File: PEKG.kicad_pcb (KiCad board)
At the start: 2 copper layers, 90 x 45 mm, 108 parts, among them J1 AudioJack4, J2 AudioJack3, U1 TL072, U12 NCS21802DMR2G, U13 NCS21802DMR2G, U2 TL072, U3 INA350CDSIDDFR, U7 TLV61070ADBVR, U8 NCS21802DMR2G

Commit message: dfs
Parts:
- BT1: footprint Battery:BatteryHolder_Keystone_2462_2xAA -> PEKG:battery_holder
- moved BT1 3.01 mm to (120.2, 129.6)
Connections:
- C47 pad 2: Net-(U7-EN) -> VBAT
- L2 pad 1: Net-(U7-EN) -> VBAT
- L3 pad 1: Net-(U7-EN) -> VBAT
- U7 pad 3: Net-(U7-EN) -> VBAT
- U7 pad 6: Net-(U7-EN) -> VBAT
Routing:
- net GND: vias 0 -> 171
- net (no net): vias 171 -> 0

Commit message: Schematic done.
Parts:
- removed C48: 10u, Resistor_SMD:R_1206_3216Metric_Pad1.30x1.75mm_HandSolder
- removed L2: 4.7u, Inductor_THT:L_Radial_D7.5mm_P3.50mm_Fastron_07P
- removed TP10: TestPoint, TestPoint:TestPoint_Pad_D3.0mm
- added JP10: Jumper_2_Open, Jumper:SolderJumper-2_P1.3mm_Open_RoundedPad1.0x1.5mm, F.Cu at (141.8, 119.1)
- added JP9: Jumper_2_Bridged, Jumper:SolderJumper-2_P1.3mm_Bridged_RoundedPad1.0x1.5mm, F.Cu at (135.3, 128.7)
- added R12: 10k, Resistor_SMD:R_0603_1608Metric_Pad0.98x0.95mm_HandSolder, F.Cu at (186.2, 128.6)
- added R2: 100, Resistor_SMD:R_0603_1608Metric_Pad0.98x0.95mm_HandSolder, F.Cu at (182.9, 128.6)
- C46, G***, U3: moved to F.Cu
- J1: footprint Connector_Audio:Jack_3.5mm_CUI_SJ1-3524N_Horizontal -> PEKG:Jack_3.5mm_4pole
- J2: value AudioJack3 -> AudioJack3_SwitchTR; footprint PEKG:Jack_3.5mm_CUI_SJ1-3523N_Horizontal -> PEKG:Jack_3.5mm_CUI_SJ1-3525N_Horizontal
- U1, U2: value TL072 -> TLV9062
- U7: footprint Package_TO_SOT_SMD:SOT-23-6 -> Package_TO_SOT_SMD:SOT-23-6_Handsoldering
- moved TP6 87.3 mm to (122.5, 133.2)
- moved TP8 86.9 mm to (122.5, 141.2)
- moved TP9 85.8 mm to (122.5, 137.2)
- moved R60 83.3 mm to (134.5, 122.1), turned to 90 degrees
- moved TP7 81.3 mm to (126.7, 120.3)
- moved TP5 80.9 mm to (125.3, 113.0)
- moved R61 68.1 mm to (149.7, 123.2), turned to 90 degrees
- moved TP4 67.7 mm to (135.3, 133.2)
- moved TP3 64.9 mm to (139.0, 114.4)
- moved TP11 61.5 mm to (152.7, 127.2)
- moved R59 55.2 mm to (162.9, 112.9), turned to -90 degrees
- moved R58 53.5 mm to (164.4, 112.9), turned to -90 degrees
- moved U7 41.3 mm to (169.0, 132.2), turned to 180 degrees
- moved R63 40.5 mm to (171.6, 129.6), turned to 180 degrees
- moved R62 37.0 mm to (168.3, 129.6), turned to 180 degrees
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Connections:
- net 2.5V renamed V_{ref}
- net Net-(JP8-A) renamed /SW_OUT
- net Net-(U7-FB) renamed /FB
- net Net-(U7-SW) renamed /SW
- net VBUS renamed V_{cc}
- C15 pad 1: GAIN_500_OUTPUT -> Net-(JP9-A)
- C21 pad 1: GAIN_500_OUTPUT -> Net-(JP10-A)
- C22 pad 1: Earth -> GND
- C41 pad 1: Earth -> GND
- C47 pad 1: Earth -> GND
- R29 pad 2: GAIN_500_OUTPUT -> Net-(JP9-A)
- R57 pad 2: GAIN_500_OUTPUT -> Net-(JP10-A)
- R61 pad 2: GAIN_500_OUTPUT -> Net-(JP10-A)
- R63 pad 1: Earth -> GND
- TP4 pad 1: GAIN_500_OUTPUT -> Net-(JP9-A)
- U1 pad 7: GAIN_500_OUTPUT -> Net-(JP10-A)
- U12 pad 1: GAIN_500_OUTPUT -> Net-(JP9-A)
- U7 pad 2: Earth -> GND
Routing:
- net /TOP: track 0.00 -> 53.7 mm, vias 0 -> 3
- net /BOTTOM: track 0.00 -> 39.2 mm, vias 0 -> 2
- net COMMON_INPUT_LEVEL: track 0.00 -> 36.8 mm, vias 0 -> 2
- net V_{ref}: track 0.00 -> 35.0 mm, vias 0 -> 4
- net RIGHT_LEG_DRIVE: track 0.00 -> 24.8 mm
- net /LA_IN: track 0.00 -> 22.6 mm, vias 0 -> 2
- net DC_COMPENSATION: track 0.00 -> 19.2 mm, vias 0 -> 2
- net /RA_IN: track 0.00 -> 18.2 mm, vias 0 -> 2
- net Net-(JP9-A): track 0.00 -> 9.89 mm
- net RIGHT_ARM: track 0.00 -> 9.76 mm
- net Net-(U13A-+): track 0.00 -> 7.90 mm
- net Net-(U8B--): track 0.00 -> 7.00 mm
- net LEFT_ARM: track 0.00 -> 6.67 mm
- net Net-(U8A--): track 0.00 -> 6.45 mm
- net Net-(U12A-+): track 0.00 -> 6.25 mm
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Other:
- board text added: "INPUT"
- board text added: "OUTPUT"

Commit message: Rutiranje gotovo.
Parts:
- moved TP3 14.7 mm to (153.3, 111.1)
- moved C17 0.13 mm to (157.0, 110.4)
- moved C18 0.13 mm to (157.0, 111.9)
- moved R33 0.13 mm to (160.4, 110.4)
- moved R37 0.13 mm to (160.4, 111.9)
- moved R26 0.10 mm to (134.5, 125.4)
- moved R34 0.09 mm to (160.4, 114.9)
- moved R38 0.09 mm to (160.4, 116.4)
- moved C19 0.07 mm to (160.4, 117.9)
- moved C20 0.07 mm to (160.4, 119.4)
- moved R36 0.06 mm to (157.0, 116.4)
- moved R39 0.06 mm to (157.0, 119.4)
- moved R40 0.06 mm to (157.0, 117.9)
- moved R56 0.06 mm to (157.0, 114.9)
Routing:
- net V_{cc}: track 3.75 -> 186.0 mm, vias 1 -> 11
- net VBAT: track 0.00 -> 68.5 mm, vias 0 -> 2
- net V_{ref}: track 35.0 -> 95.3 mm
- net FIL_OUT: track 0.00 -> 43.5 mm, vias 0 -> 4
- net GAIN_5000_OUTPUT: track 0.00 -> 38.7 mm, vias 0 -> 2
- net LEVELED_OUTPUT: track 0.00 -> 31.6 mm
- net GAIN_50_OUTPUT: track 0.00 -> 30.3 mm, vias 0 -> 2
- net DC_COMPENSATION: track 19.2 -> 43.1 mm, vias 2 -> 4
- net GND: track 1.02 -> 20.9 mm, vias 172 -> 190
- net Net-(U2A--): track 0.00 -> 14.0 mm, vias 0 -> 2
- net GAIN_500_OUTPUT: track 2.00 -> 13.7 mm
- net Net-(U2B--): track 0.00 -> 11.3 mm
- net Net-(JP2-A): track 0.00 -> 10.5 mm
- net Net-(JP10-A): track 0.00 -> 10.2 mm
- net Net-(C17-Pad1): track 0.00 -> 9.05 mm
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- added copper zone on F.Cu, net /SW
- added copper zone on F.Cu, net /SW_OUT
- added copper zone on B.Cu, net GND
- added copper zone on F.Cu, net GND
- added copper zone on F.Cu, net VBAT

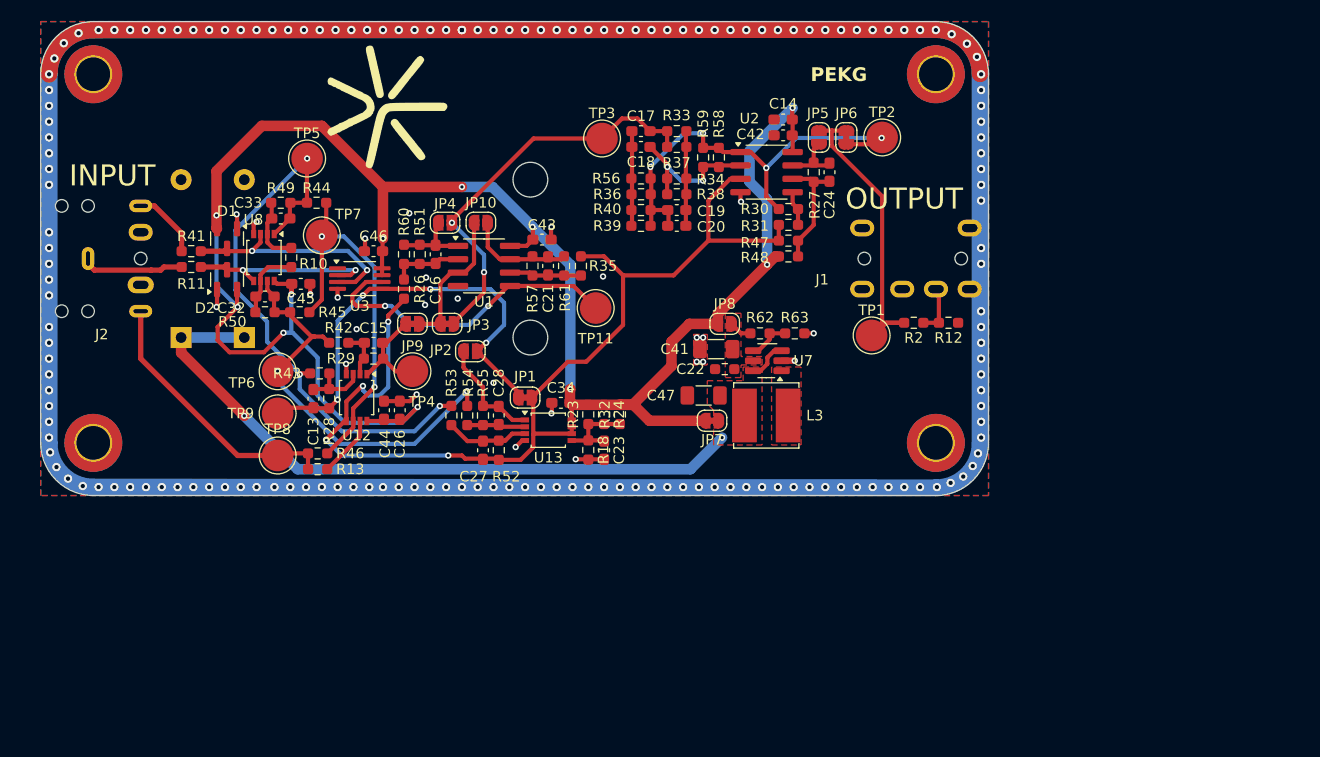
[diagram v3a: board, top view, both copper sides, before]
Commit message: Rounded traces??? fixed silkscreen.
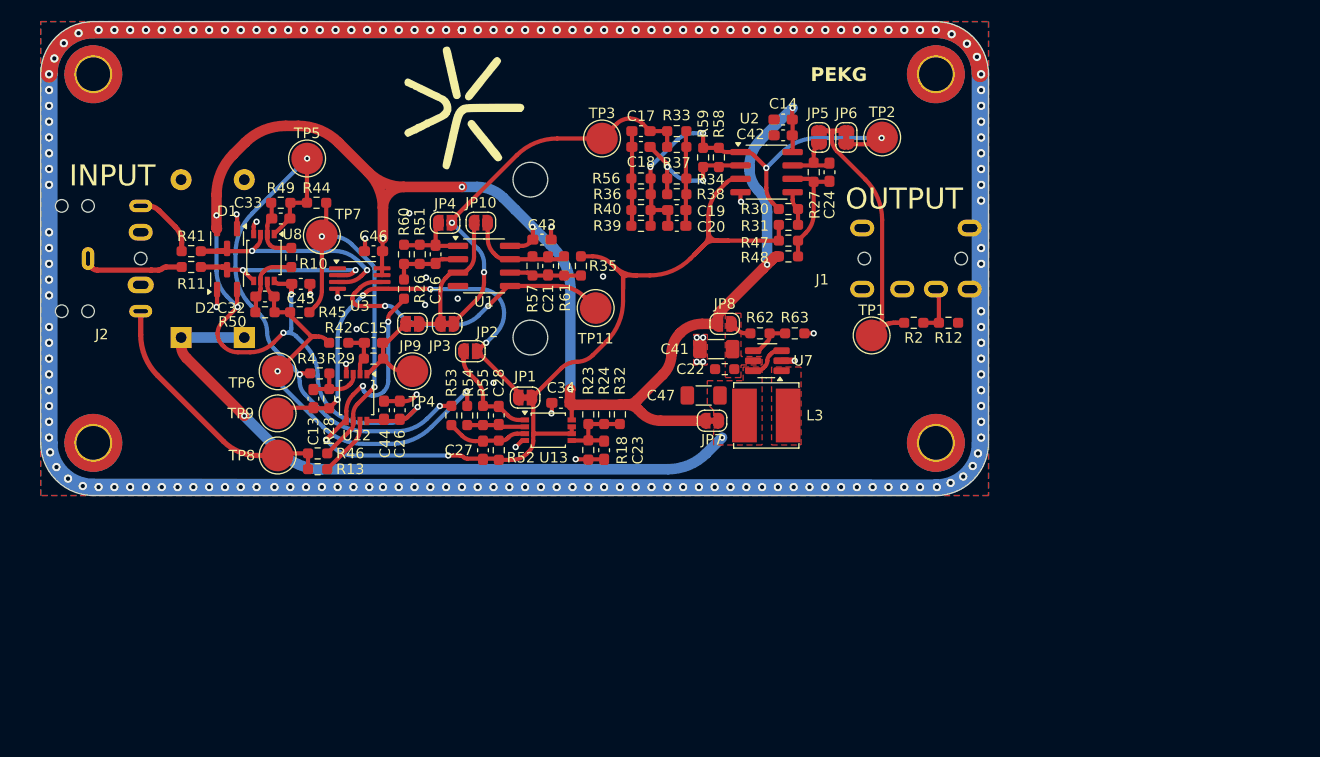
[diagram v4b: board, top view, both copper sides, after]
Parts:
- moved G*** 7.30 mm to (140.2, 108.2)
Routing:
- net V_{ref}: track 95.3 -> 102.2 mm
- net /TOP: track 54.7 -> 53.4 mm
- net /BOTTOM: track 39.6 -> 38.8 mm
- net VBAT: track 68.5 -> 67.7 mm
- net GAIN_50_OUTPUT: track 30.3 -> 29.6 mm
- net DC_COMPENSATION: track 43.1 -> 42.4 mm
- net GAIN_5000_OUTPUT: track 38.7 -> 38.1 mm
- net FIL_OUT: track 43.5 -> 42.9 mm
- net RIGHT_LEG_DRIVE: track 25.8 -> 25.3 mm

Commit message: Updated leg drive, output connector, boost converter.
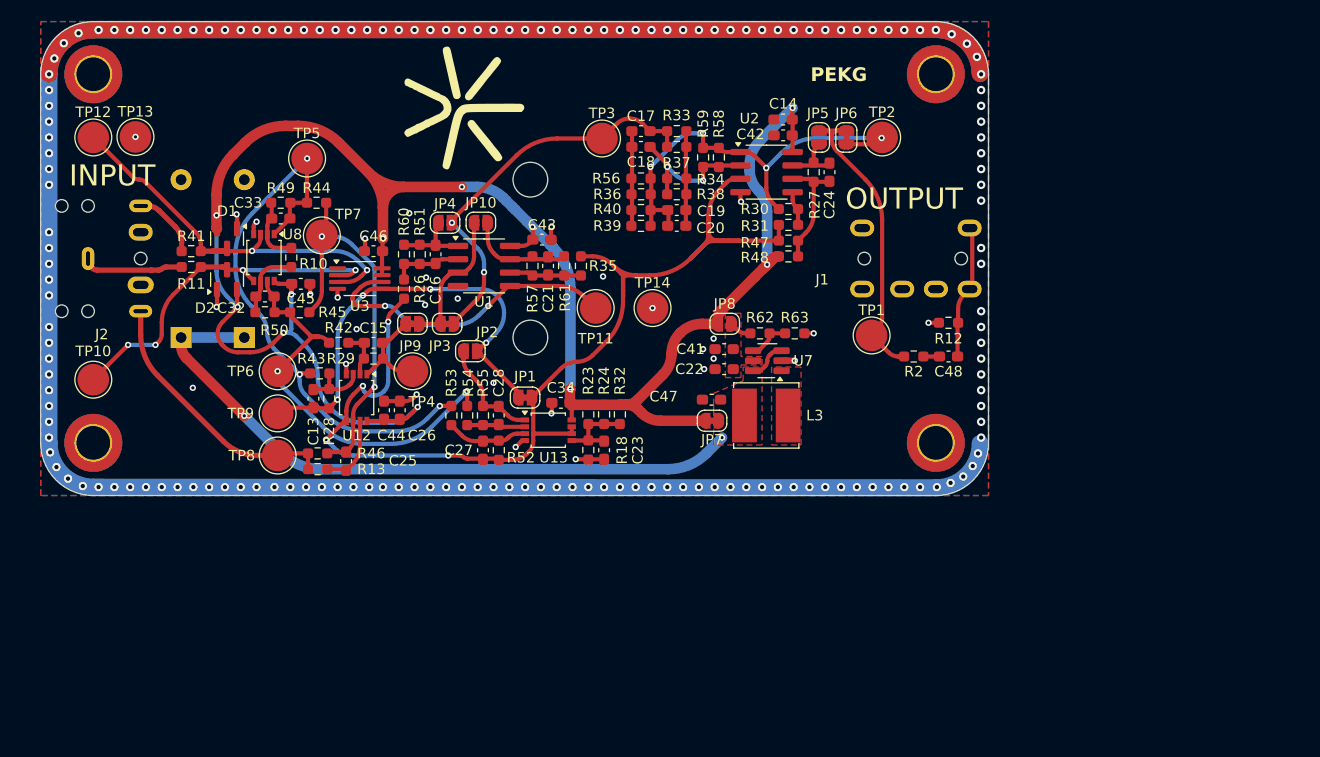
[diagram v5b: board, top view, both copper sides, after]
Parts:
- added C25: 10n, Capacitor_SMD:C_0603_1608Metric_Pad1.08x0.95mm_HandSolder, F.Cu at (129.0, 141.7)
- added C48: 10u, Capacitor_SMD:C_0603_1608Metric_Pad1.08x0.95mm_HandSolder, F.Cu at (186.2, 131.8)
- added TP10: TestPoint, TestPoint:TestPoint_Pad_D3.0mm, F.Cu at (105.0, 134.0)
- added TP12: TestPoint, TestPoint:TestPoint_Pad_D3.0mm, F.Cu at (105.0, 111.0)
- added TP13: TestPoint, TestPoint:TestPoint_Pad_D3.0mm, F.Cu at (109.0, 111.0)
- added TP14: TestPoint, TestPoint:TestPoint_Pad_D3.0mm, F.Cu at (158.1, 127.2)
- C22: value 1u -> 10u; footprint Resistor_SMD:R_0603_1608Metric_Pad0.98x0.95mm_HandSolder -> Capacitor_SMD:C_0603_1608Metric_Pad1.08x0.95mm_HandSolder
- C41, C47: footprint Resistor_SMD:R_1206_3216Metric_Pad1.30x1.75mm_HandSolder -> Capacitor_SMD:C_0603_1608Metric_Pad1.08x0.95mm_HandSolder
- moved R2 3.20 mm to (182.9, 131.8)
- moved C47 0.85 mm to (163.7, 135.9)
- moved C41 0.75 mm to (164.9, 131.1)
- turned R12 to 0 degrees
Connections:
- J1 pad R2: Net-(J1-PadR2) -> GND
- J1 pad S: GND -> Net-(C48-Pad1)
- R12 pad 2: Net-(J1-PadR2) -> Net-(C48-Pad1)
- R2 pad 1: Net-(J1-PadR2) -> Net-(C48-Pad2)
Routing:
- net /RA_IN: track 18.1 -> 34.3 mm, vias 2 -> 4
- net /LA_IN: track 22.5 -> 38.2 mm
- net Net-(C48-Pad1): track 0.00 -> 12.7 mm
- net Net-(J1-PadR2): track 4.77 -> 0.00 mm
- net LEVELED_OUTPUT: track 32.1 -> 29.2 mm
- net V_{ref}: track 102.2 -> 104.7 mm
- net Net-(C48-Pad2): track 0.00 -> 1.53 mm
- net Net-(C25-Pad2): track 5.78 -> 6.90 mm
- net GND: track 20.8 -> 21.8 mm, vias 190 -> 193
- net COMMON_INPUT_LEVEL: track 36.4 -> 37.4 mm

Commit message: Updated input conn, updated battery holder.
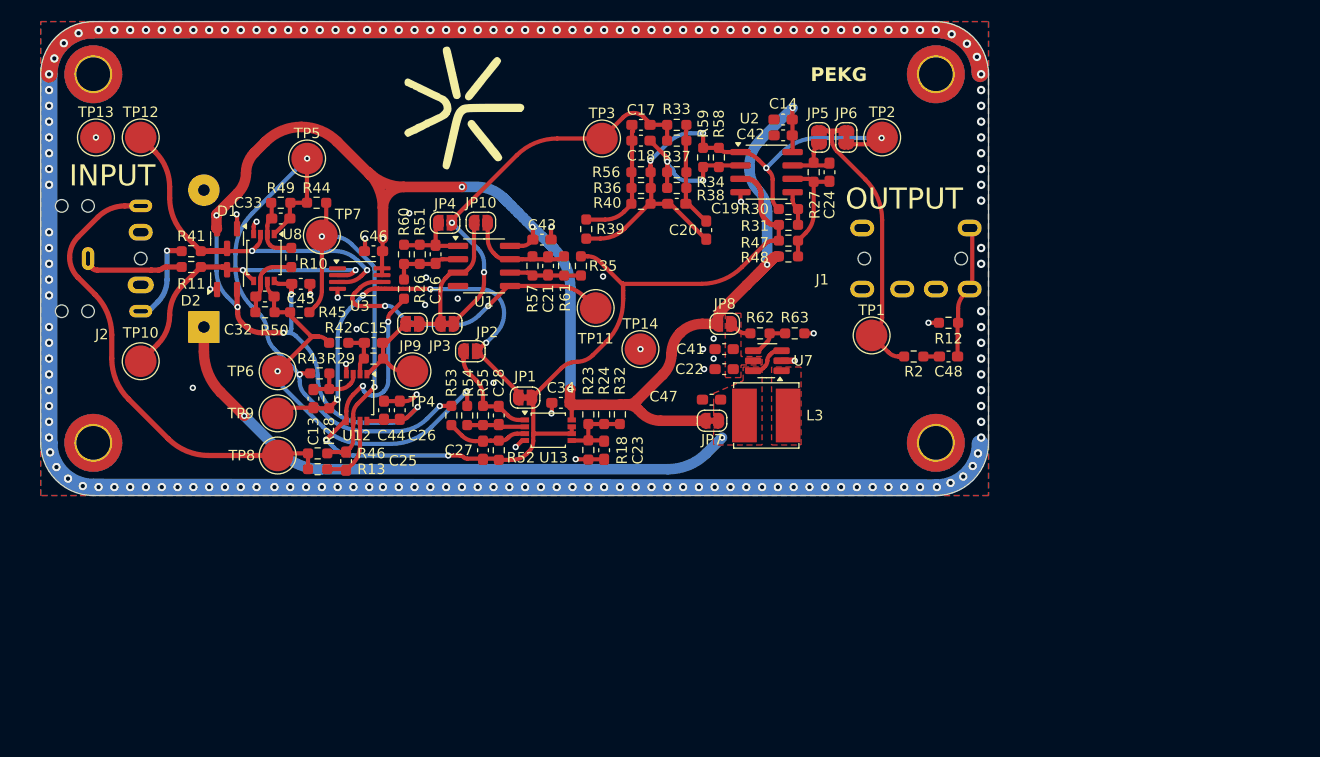
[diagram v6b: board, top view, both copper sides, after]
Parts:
- BT1: footprint PEKG:battery_holder -> PEKG:MG_battery_holder
- moved R39 5.21 mm to (151.8, 119.7), turned to 90 degrees
- moved BT1 5.00 mm to (141.5, 122.5)
- moved TP10 4.83 mm to (109.5, 132.2)
- moved TP12 4.50 mm to (109.5, 111.0)
- moved TP14 4.07 mm to (156.9, 131.1)
- moved TP13 3.75 mm to (105.2, 111.0)
- moved C20 2.83 mm to (163.2, 119.8), turned to 90 degrees
- moved C17 0.59 mm to (157.0, 109.8)
- moved C18 0.59 mm to (157.0, 111.3)
- moved C19 0.59 mm to (160.4, 117.3)
- moved R33 0.59 mm to (160.4, 109.8)
- moved R34 0.59 mm to (160.4, 114.3)
- moved R36 0.59 mm to (157.0, 115.8)
- moved R37 0.59 mm to (160.4, 111.3)
- moved R38 0.59 mm to (160.4, 115.8)
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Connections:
- J2 pad R: LEFT_ARM -> RIGHT_LEG_DRIVE
- J2 pad T: RIGHT_LEG_DRIVE -> LEFT_ARM
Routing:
- net RIGHT_LEG_DRIVE: track 25.3 -> 44.8 mm
- net V_{ref}: track 104.7 -> 94.1 mm
- net FIL_OUT: track 42.9 -> 51.8 mm
- net VBAT: track 67.7 -> 61.6 mm
- net V_{cc}: track 185.7 -> 179.8 mm
- net /RA_IN: track 34.3 -> 29.0 mm, vias 4 -> 2
- net Net-(C17-Pad1): track 9.04 -> 11.8 mm
- net /LA_IN: track 38.2 -> 35.8 mm
- net LEFT_ARM: track 6.50 -> 8.44 mm, vias 0 -> 1
- net GND: track 21.8 -> 20.8 mm
- net Net-(C19-Pad2): track 9.01 -> 9.57 mm

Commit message: all hail JFET.
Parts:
- moved G*** 1.45 mm to (138.8, 108.2), turned to 0 degrees
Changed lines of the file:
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@@
 			(outputformat 1)
 			(mirror no)
-			(drillshape 1)
+			(drillshape 0)
 			(scaleselection 1)
-			(outputdirectory "")
+			(outputdirectory "gerbers/")
 		)
 	)
@@
 		(locked yes)
 		(layer "F.Cu")
-		(at 140.2 108.2 180)
+		(at 138.75 108.2)
 		(property "Reference" "G***"
-			(at 0 0 180)
+			(at 0 0 0)
 			(layer "F.SilkS")
 			(hide yes)
@@
 		)
 		(property "Value" "LOGO"
-			(at 0.75 0 180)
+			(at 0.75 0 0)
 			(layer "F.SilkS")
 			(hide yes)
@@
 		)
 		(property "Datasheet" ""
-			(at 0 0 180)
+			(at 0 0 0)
 			(layer "F.Fab")
 			(hide yes)
@@
 		)
 		(property "Description" ""
-			(at 0 0 180)
+			(at 0 0 0)
 			(layer "F.Fab")
 			(hide yes)

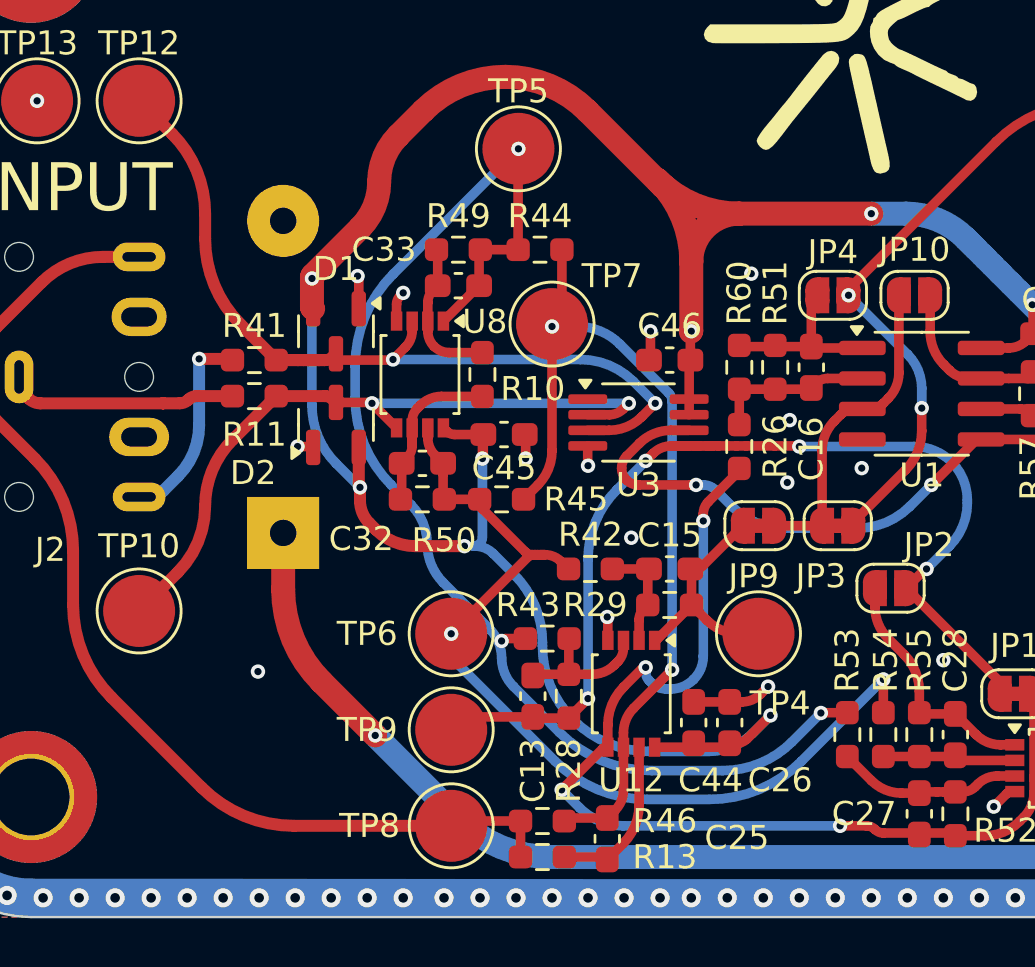
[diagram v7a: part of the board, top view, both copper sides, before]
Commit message: Fixed inverted DC off, reduced gain from 500 to 5
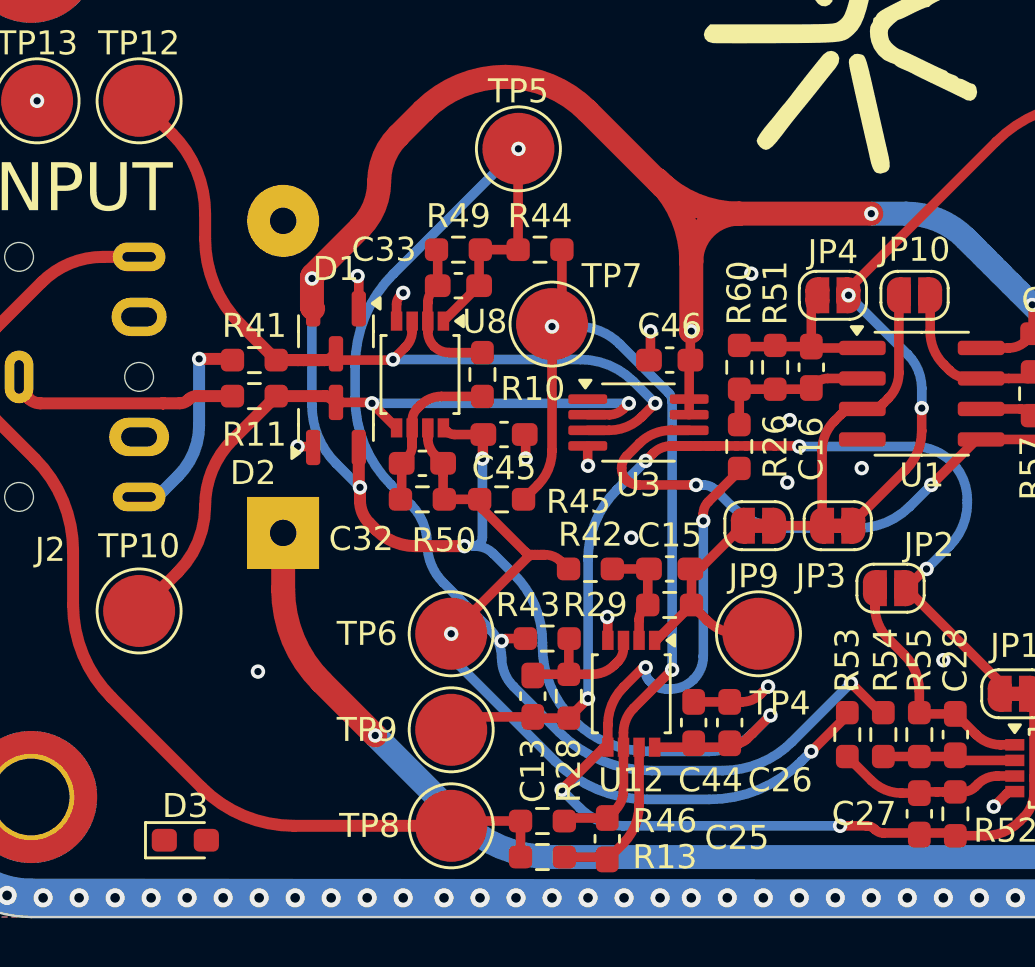
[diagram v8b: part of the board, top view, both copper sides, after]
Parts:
- added D3: LED, LED_SMD:LED_0603_1608Metric_Pad1.05x0.95mm_HandSolder, F.Cu at (111.4, 141.8)
- R42, R43: value 1k -> 100k
- R44, R45, R46: value 1k -> 10k
- turned R44 to 180 degrees
- turned R45 to 0 degrees
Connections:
- R44 pad 1: /TOP -> COMMON_INPUT_LEVEL
- R44 pad 2: COMMON_INPUT_LEVEL -> /TOP
- R45 pad 1: COMMON_INPUT_LEVEL -> /BOTTOM
- R45 pad 2: /BOTTOM -> COMMON_INPUT_LEVEL
- R53 pad 1: /TOP -> /BOTTOM
- R54 pad 1: /BOTTOM -> /TOP
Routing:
- net /BOTTOM: track 39.1 -> 35.7 mm
- net /TOP: track 53.4 -> 55.8 mm
